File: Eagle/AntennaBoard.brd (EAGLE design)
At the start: 89.8 x 59.7 mm, 18 parts, among them IC1 MEGA8-P, IC2 MAX485, IC3 7805

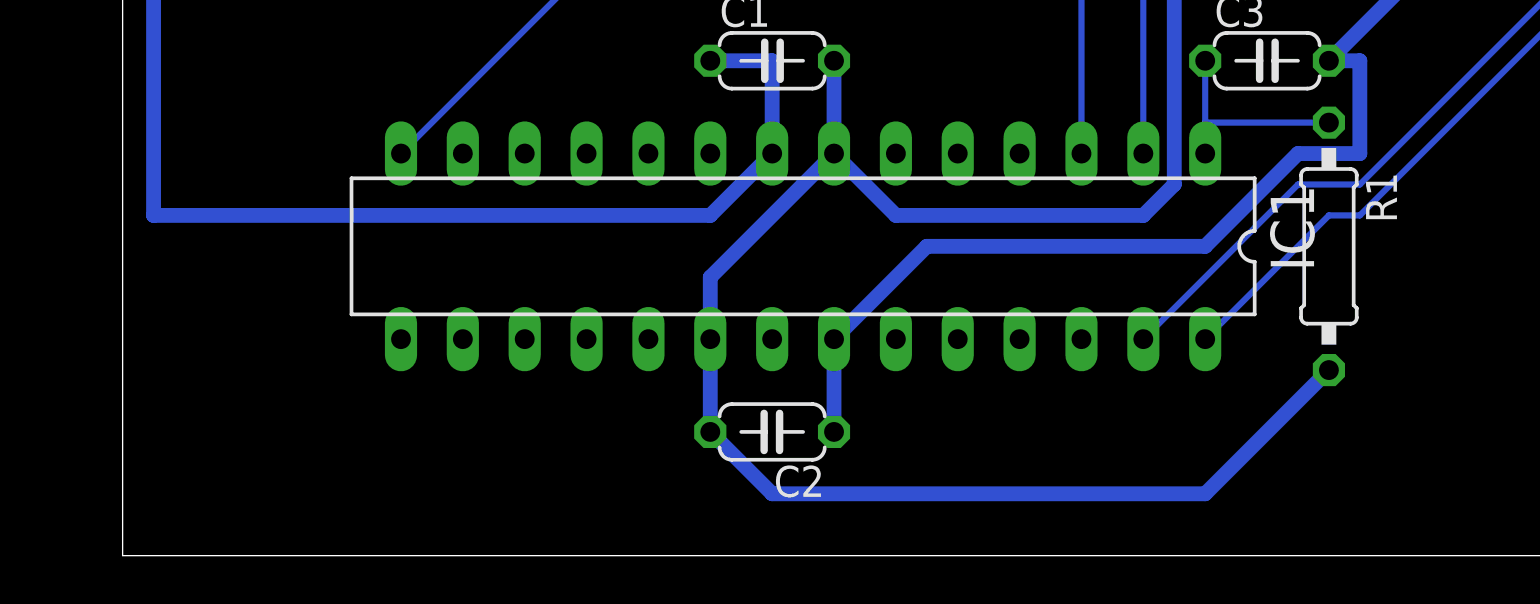
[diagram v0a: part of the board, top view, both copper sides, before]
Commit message: - IPS-Header added to AntennaBoard, U.Radig layout
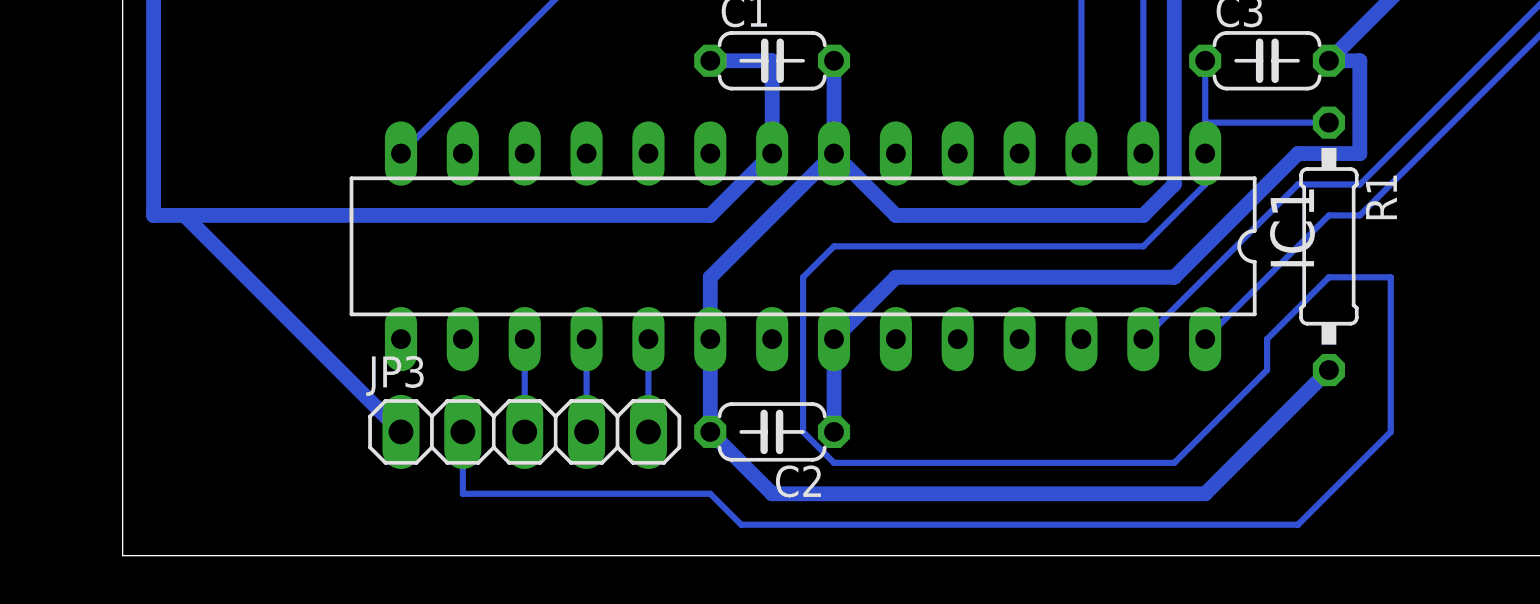
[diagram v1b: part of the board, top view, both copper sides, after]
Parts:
- added JP3: (no value), pinhead:1X05
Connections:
- new net N$13: IC1.17, JP3.3
- new net N$14: IC1.18, JP3.4
- new net N$15: IC1.19, JP3.5
- net GND: now also JP3.1
- net N$5: now also JP3.2
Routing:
- net N$5: track 8.89 -> 112.2 mm
- net GND: track 301.8 -> 314.3 mm
- net N$15: track 0.00 -> 3.81 mm
- net N$14: track 0.00 -> 3.81 mm
- net N$13: track 0.00 -> 3.81 mm
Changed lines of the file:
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@@
 <element name="L1" library="rcl" package="0207/12" value="100u" x="15.24" y="39.37"/>
 <element name="L2" library="rcl" package="0207/12" value="100u" x="15.24" y="44.45"/>
+<element name="JP3" library="pinhead" package="1X05" value="" x="16.51" y="13.97"/>
 </elements>
 <signals>
@@
 <wire x1="71.12" y1="50.8" x2="49.53" y2="29.21" width="0.6096" layer="16"/>
 <wire x1="71.12" y1="52.07" x2="71.12" y2="50.8" width="0.254" layer="16"/>
-<wire x1="33.02" y1="21.59" x2="29.21" y2="17.78" width="0.6096" layer="16"/>
-<wire x1="44.45" y1="21.59" x2="33.02" y2="21.59" width="0.6096" layer="16"/>
-<wire x1="48.26" y1="25.4" x2="44.45" y2="21.59" width="0.6096" layer="16"/>
+<wire x1="31.75" y1="20.32" x2="29.21" y2="17.78" width="0.6096" layer="16"/>
+<wire x1="43.18" y1="20.32" x2="31.75" y2="20.32" width="0.6096" layer="16"/>
+<wire x1="48.26" y1="25.4" x2="43.18" y2="20.32" width="0.6096" layer="16"/>
 <wire x1="50.8" y1="25.4" x2="48.26" y2="25.4" width="0.6096" layer="16"/>
 <wire x1="50.8" y1="29.21" x2="50.8" y2="25.4" width="0.6096" layer="16"/>
@@
 <wire x1="1.27" y1="22.86" x2="1.27" y2="36.83" width="0.6096" layer="16"/>
 <wire x1="1.27" y1="36.83" x2="1.27" y2="59.69" width="0.6096" layer="16"/>
-<wire x1="24.13" y1="22.86" x2="1.27" y2="22.86" width="0.6096" layer="16"/>
+<wire x1="24.13" y1="22.86" x2="2.54" y2="22.86" width="0.6096" layer="16"/>
+<wire x1="2.54" y1="22.86" x2="1.27" y2="22.86" width="0.6096" layer="16"/>
 <wire x1="26.67" y1="25.4" x2="24.13" y2="22.86" width="0.6096" layer="16"/>
 <wire x1="20.32" y1="45.72" x2="27.94" y2="45.72" width="0.6096" layer="16"/>
@@
 <wire x1="12.7" y1="57.15" x2="17.78" y2="57.15" width="0.6096" layer="16"/>
 <wire x1="1.27" y1="36.83" x2="5.08" y2="36.83" width="0.6096" layer="16"/>
+<contactref element="JP3" pad="1"/>
+<wire x1="2.54" y1="22.86" x2="11.43" y2="13.97" width="0.6096" layer="16"/>
 </signal>
 <signal name="N$5">
@@
 <wire x1="44.45" y1="26.67" x2="49.53" y2="26.67" width="0.254" layer="16"/>
 <wire x1="44.45" y1="26.67" x2="44.45" y2="25.4" width="0.254" layer="16"/>
+<contactref element="JP3" pad="2"/>
+<wire x1="44.45" y1="25.4" x2="44.45" y2="24.13" width="0.254" layer="16"/>
+<wire x1="44.45" y1="24.13" x2="41.91" y2="21.59" width="0.254" layer="16"/>
+<wire x1="41.91" y1="21.59" x2="29.21" y2="21.59" width="0.254" layer="16"/>
+<wire x1="29.21" y1="21.59" x2="27.94" y2="20.32" width="0.254" layer="16"/>
+<wire x1="27.94" y1="20.32" x2="27.94" y2="13.97" width="0.254" layer="16"/>
+<wire x1="27.94" y1="13.97" x2="29.21" y2="12.7" width="0.254" layer="16"/>
+<wire x1="29.21" y1="12.7" x2="43.18" y2="12.7" width="0.254" layer="16"/>
+<wire x1="43.18" y1="12.7" x2="46.99" y2="16.51" width="0.254" layer="16"/>
+<wire x1="46.99" y1="16.51" x2="46.99" y2="17.78" width="0.254" layer="16"/>
+<wire x1="46.99" y1="17.78" x2="49.53" y2="20.32" width="0.254" layer="16"/>
+<wire x1="49.53" y1="20.32" x2="52.07" y2="20.32" width="0.254" layer="16"/>
+<wire x1="52.07" y1="20.32" x2="52.07" y2="13.97" width="0.254" layer="16"/>
+<wire x1="52.07" y1="13.97" x2="48.26" y2="10.16" width="0.254" layer="16"/>
+<wire x1="48.26" y1="10.16" x2="25.4" y2="10.16" width="0.254" layer="16"/>
+<wire x1="25.4" y1="10.16" x2="24.13" y2="11.43" width="0.254" layer="16"/>
+<wire x1="24.13" y1="11.43" x2="13.97" y2="11.43" width="0.254" layer="16"/>
+<wire x1="13.97" y1="11.43" x2="13.97" y2="13.97" width="0.254" layer="16"/>
 </signal>
 <signal name="+5V">
@@
 </signal>
 <signal name="N$7">
+<contactref element="IC1" pad="14"/>
 <contactref element="IC2" pad="2"/>
 <contactref element="IC2" pad="3"/>
-<contactref element="IC1" pad="14"/>
 <wire x1="21.59" y1="35.56" x2="11.43" y2="25.4" width="0.254" layer="16"/>
 <wire x1="29.21" y1="35.56" x2="21.59" y2="35.56" width="0.254" layer="16"/>
@@
 <wire x1="2.54" y1="39.37" x2="2.54" y2="41.91" width="0.254" layer="16"/>
 </signal>
+<signal name="N$13">
+<contactref element="IC1" pad="17"/>
+<contactref element="JP3" pad="3"/>
+<wire x1="16.51" y1="13.97" x2="16.51" y2="17.78" width="0.254" layer="16"/>
+</signal>
+<signal name="N$14">
+<contactref element="JP3" pad="4"/>
+<contactref element="IC1" pad="18"/>
+<wire x1="19.05" y1="13.97" x2="19.05" y2="17.78" width="0.254" layer="16"/>
+</signal>
+<signal name="N$15">
+<contactref element="IC1" pad="19"/>
+<contactref element="JP3" pad="5"/>
+<wire x1="21.59" y1="13.97" x2="21.59" y2="17.78" width="0.254" layer="16"/>
+</signal>
 </signals>

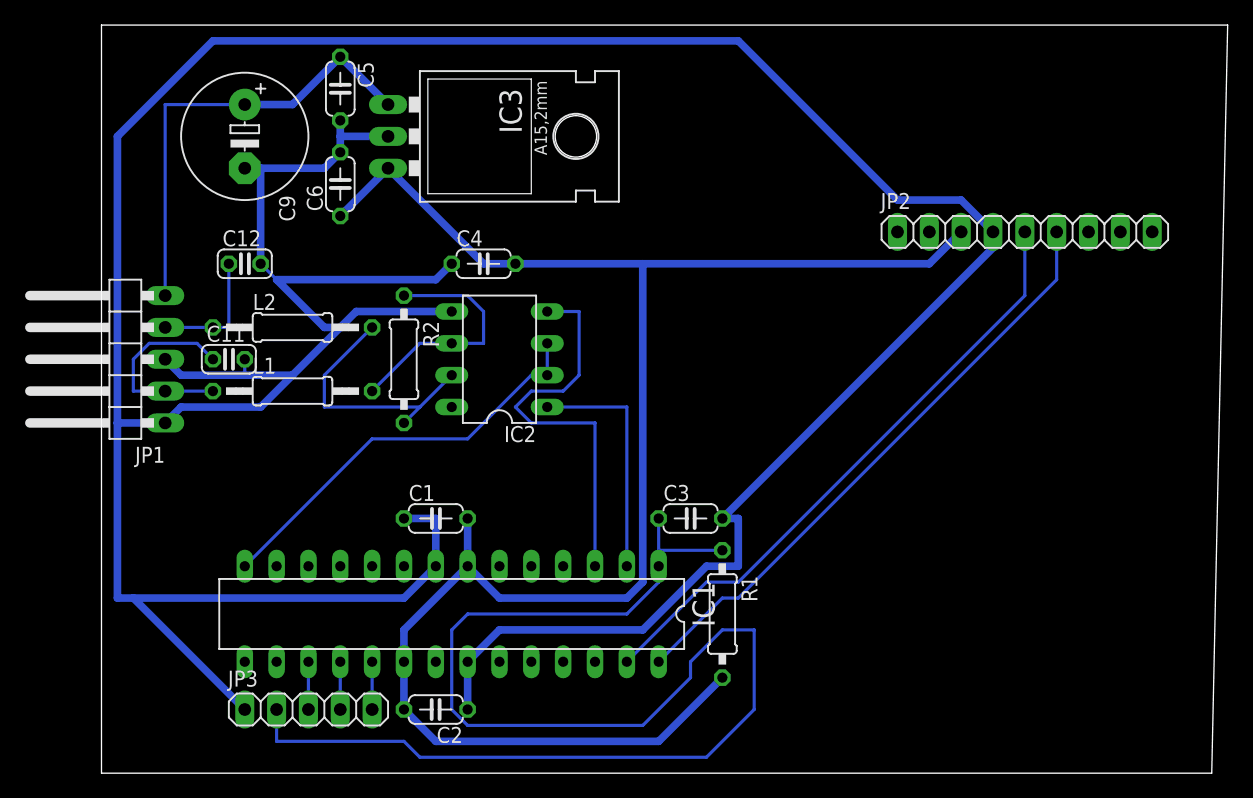
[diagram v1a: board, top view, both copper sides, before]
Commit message: - AntennaBoard: ERC errors fixed, worked on board and DRC - PowerSupply: ERC & DRC errors fixed
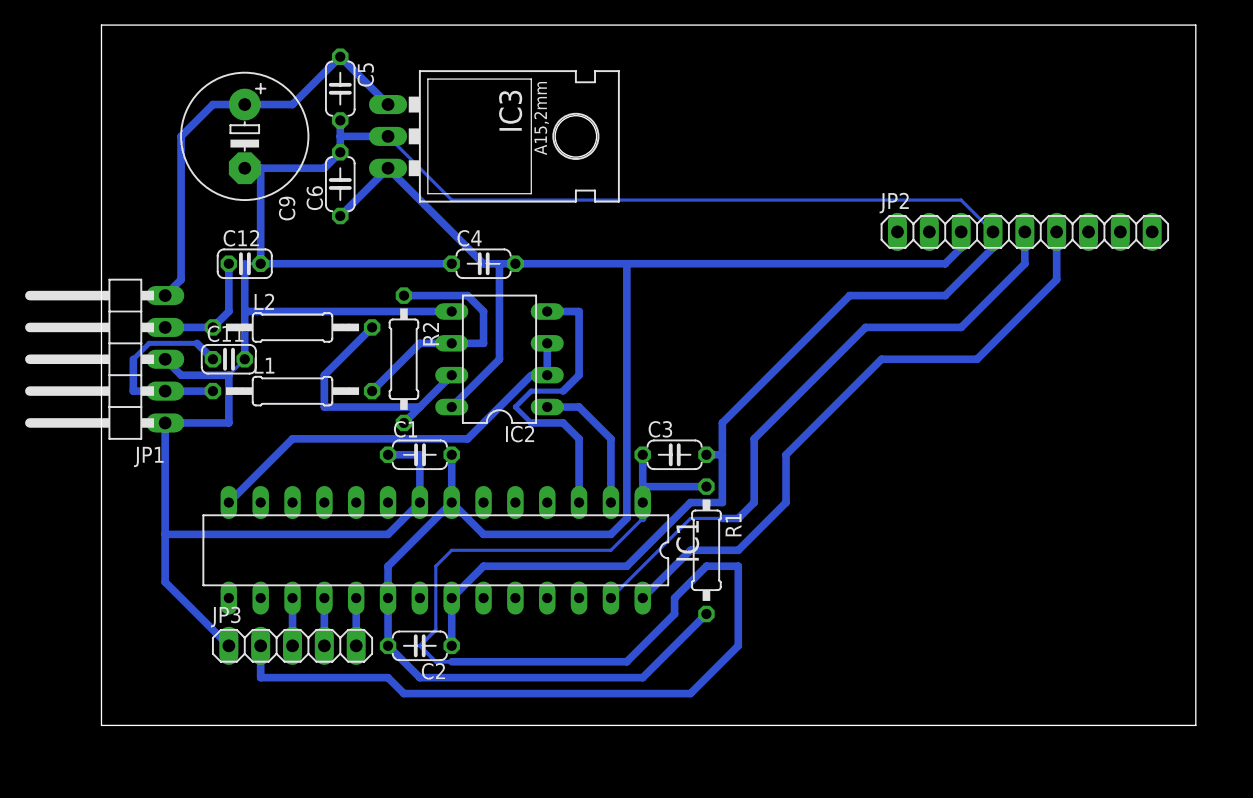
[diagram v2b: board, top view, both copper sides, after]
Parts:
- C9: value (none) -> 220u
- moved IC1 5.24 mm to (26.7, 26.7)
- moved R1 5.24 mm to (48.3, 26.7)
- moved C1 5.24 mm to (25.4, 34.3)
- moved C2 5.24 mm to (25.4, 19.1)
- moved C3 5.24 mm to (45.7, 34.3)
- moved JP3 5.24 mm to (15.2, 19.1)
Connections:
- removed net VCC: IC2.8
- net +5V: now also IC2.8
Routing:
- net GND: track 314.3 -> 242.9 mm
- net +5V: track 142.2 -> 150.8 mm
- net N$8: track 19.0 -> 11.2 mm
- net N$9: track 32.1 -> 25.0 mm
- net N$1: track 36.2 -> 33.9 mm
- net N$5: track 112.2 -> 114.0 mm
- net N$4: track 48.2 -> 49.6 mm
- net N$7: track 33.0 -> 32.1 mm
- net N$3: track 10.2 -> 9.42 mm
- net N$6: track 48.9 -> 49.6 mm
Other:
- board size 89.8 x 59.7 mm -> 87.3 x 55.9 mm
